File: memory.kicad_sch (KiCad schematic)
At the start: 18 parts, among them U2 MX25L4006EM2R-12G, U3 AT25SF128A-SHB-T

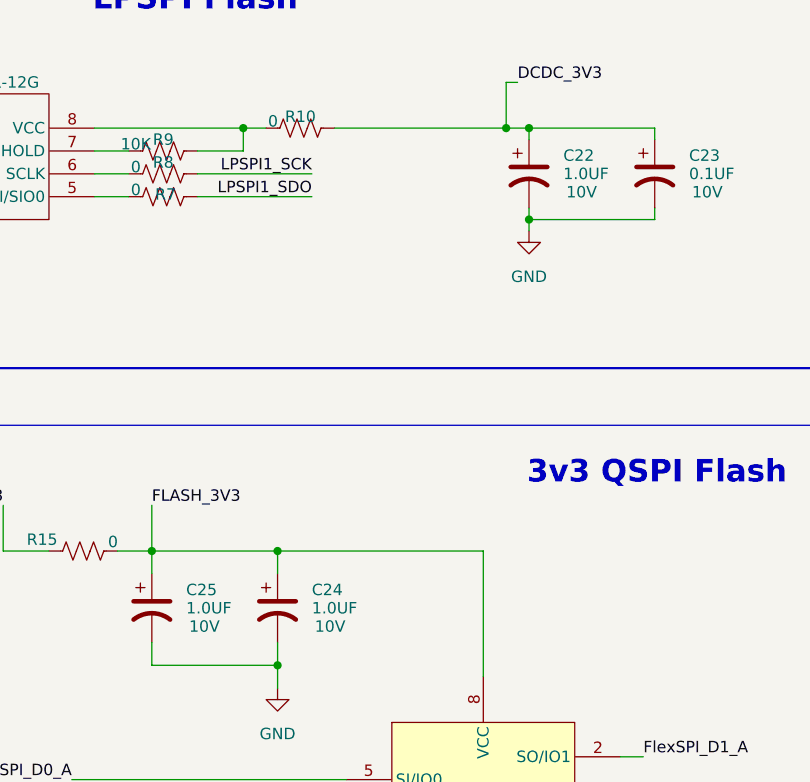
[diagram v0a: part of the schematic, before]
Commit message: menambah lebih dari setengah footprint
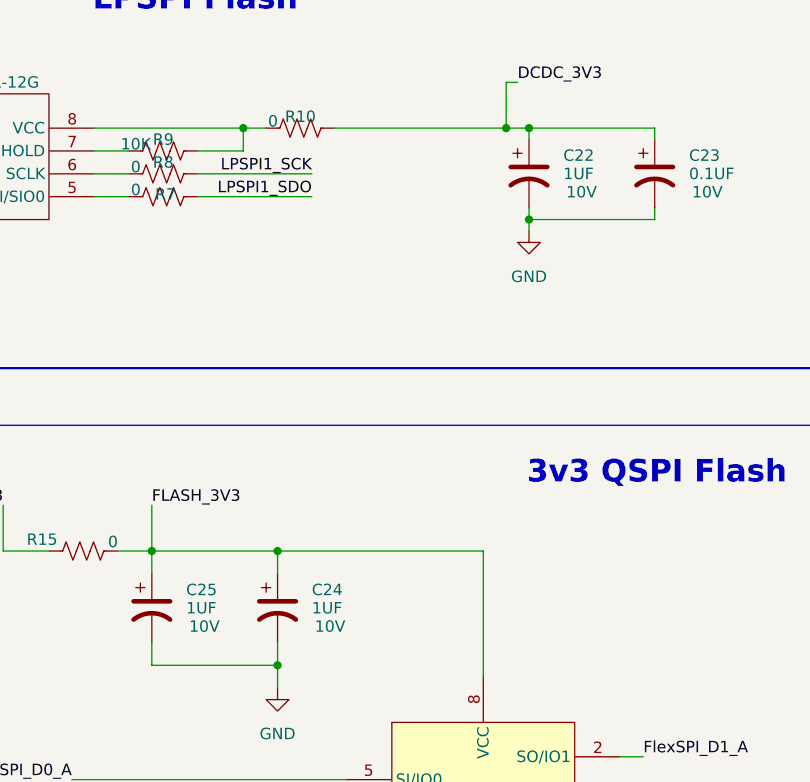
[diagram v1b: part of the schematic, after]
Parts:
- C22, C24, C25: value 1.0UF -> 1UF; footprint (none) -> Capacitor_SMD:C_0402_1005Metric
- C23: footprint (none) -> Capacitor_SMD:C_0402_1005Metric; MANUFACTURER (none) -> CC0402KRX5R6BB104
- R10, R11, R12, R13, R14, R15, R16, R17, R18, R7, R8, R9: footprint (none) -> Resistor_SMD:R_0402_1005Metric
- U2: footprint (none) -> Package_SON:WSON-8-1EP_6x5mm_P1.27mm_EP3.4x4.3mm; DigikeyPartNumber (none) -> MX25L4006EZNI-12G; MANUFACTURER (none) -> MX25L4006EZNI-12G
- U3: footprint (none) -> AT25SF128A_SHB_T:IC8_AT25SF128A-SHB-T_ADO; MANUFACTURER (none) -> AT25SF128A-SHB-T
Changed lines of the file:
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@@
 			)
 		)
-		(property "Footprint" ""
+		(property "Footprint" "AT25SF128A_SHB_T:IC8_AT25SF128A-SHB-T_ADO"
 			(at 229.87 129.54 0)
 			(effects
@@
 			)
 		)
+		(property "DigikeyPartNumber" ""
+			(at 229.87 129.54 0)
+			(effects
+				(font
+					(size 1.27 1.27)
+				)
+				(hide yes)
+			)
+		)
+		(property "MANUFACTURER" "AT25SF128A-SHB-T"
+			(at 229.87 129.54 0)
+			(effects
+				(font
+					(size 1.27 1.27)
+				)
+				(hide yes)
+			)
+		)
 		(pin "8"
 		)
@@
 			)
 		)
-		(property "Footprint" ""
+		(property "Footprint" "Resistor_SMD:R_0402_1005Metric"
 			(at 194.564 56.134 90)
 			(effects
@@
 			)
 		)
+		(property "DigikeyPartNumber" ""
+			(at 194.31 57.15 0)
+			(effects
+				(font
+					(size 1.27 1.27)
+				)
+				(hide yes)
+			)
+		)
 		(pin "1"
 		)
@@
 			)
 		)
-		(property "Footprint" ""
+		(property "Footprint" "Resistor_SMD:R_0402_1005Metric"
 			(at 143.764 48.514 90)
 			(effects
@@
 			)
 		)
+		(property "DigikeyPartNumber" ""
+			(at 143.51 49.53 0)
+			(effects
+				(font
+					(size 1.27 1.27)
+				)
+				(hide yes)
+			)
+		)
 		(pin "2"
 		)
@@
 			)
 		)
-		(property "Footprint" ""
+		(property "Footprint" "Resistor_SMD:R_0402_1005Metric"
 			(at 210.566 141.224 90)
 			(effects
@@
 					(size 1.27 1.27)
 				)
+			)
+		)
+		(property "DigikeyPartNumber" ""
+			(at 209.55 140.97 0)
+			(effects
+				(font
+					(size 1.27 1.27)
+				)
+				(hide yes)
 			)
 		)
@@
 			)
 		)
-		(property "Footprint" ""
+		(property "Footprint" "Capacitor_SMD:C_0402_1005Metric"
 			(at 248.92 54.61 0)
 			(effects
@@
 			)
 		)
+		(property "DigikeyPartNumber" ""
+			(at 248.92 54.61 0)
+			(effects
+				(font
+					(size 1.27 1.27)
+				)
+				(hide yes)
+			)
+		)
+		(property "MANUFACTURER" "CC0402KRX5R6BB104"
+			(at 248.92 54.61 0)
+			(effects
+				(font
+					(size 1.27 1.27)
+				)
+				(hide yes)
+			)
+		)
 		(pin "1"
 		)
@@
 			)
 		)
-		(property "Footprint" ""
+		(property "Footprint" "Resistor_SMD:R_0402_1005Metric"
 			(at 143.764 53.594 90)
 			(effects
@@
 		)
 		(property "Description" "Resistor, US symbol"
+			(at 143.51 54.61 0)
+			(effects
+				(font
+					(size 1.27 1.27)
+				)
+				(hide yes)
+			)
+		)
+		(property "DigikeyPartNumber" ""
 			(at 143.51 54.61 0)
 			(effects
@@
 			)
 		)
-		(property "Value" "1.0UF"
+		(property "Value" "1UF"
 			(at 238.76 54.61 0)
 			(effects
@@
 			)
 		)
-		(property "Footprint" ""
+		(property "Footprint" "Capacitor_SMD:C_0402_1005Metric"
 			(at 234.95 54.61 0)
 			(effects
@@
 					(size 1.27 1.27)
 				)
+			)
+		)
+		(property "DigikeyPartNumber" ""
+			(at 234.95 54.61 0)
+			(effects
+				(font
+					(size 1.27 1.27)
+				)
+				(hide yes)
 			)
 		)
@@
 			)
 		)
-		(property "Footprint" ""
+		(property "Footprint" "Resistor_SMD:R_0402_1005Metric"
 			(at 192.786 141.224 90)
 			(effects
@@
 			)
 		)
+		(property "DigikeyPartNumber" ""
+			(at 191.77 140.97 0)
+			(effects
+				(font
+					(size 1.27 1.27)
+				)
+				(hide yes)
+			)
+		)
 		(pin "1"
 		)
@@
 			)
 		)
-		(property "Footprint" ""
+		(property "Footprint" "Resistor_SMD:R_0402_1005Metric"
 			(at 194.564 53.594 90)
 			(effects
@@
 			)
 		)
+		(property "DigikeyPartNumber" ""
+			(at 194.31 54.61 0)
+			(effects
+				(font
+					(size 1.27 1.27)
+				)
+				(hide yes)
+			)
+		)
 		(pin "1"
 		)
@@
 			)
 		)
-		(property "Footprint" ""
+		(property "Footprint" "Resistor_SMD:R_0402_1005Metric"
 			(at 201.676 141.224 90)
 			(effects
@@
 			)
 		)
+		(property "DigikeyPartNumber" ""
+			(at 200.66 140.97 0)
+			(effects
+				(font
+					(size 1.27 1.27)
+				)
+				(hide yes)
+			)
+		)
 		(pin "1"
 		)
@@
 			)
 		)
-		(property "Footprint" ""
+		(property "Footprint" "Resistor_SMD:R_0402_1005Metric"
 			(at 143.764 45.974 90)
 			(effects
@@
 			)
 		)
+		(property "DigikeyPartNumber" ""
+			(at 143.51 46.99 0)
+			(effects
+				(font
+					(size 1.27 1.27)
+				)
+				(hide yes)
+			)
+		)
 		(pin "2"
 		)
@@
 			)
 		)
-		(property "Footprint" ""
+		(property "Footprint" "Resistor_SMD:R_0402_1005Metric"
 			(at 209.804 48.514 90)
 			(effects
@@
 			)
 		)
+		(property "DigikeyPartNumber" ""
+			(at 209.55 49.53 0)
+			(effects
+				(font
+					(size 1.27 1.27)
+				)
+				(hide yes)
+			)
+		)
 		(pin "1"
 		)
@@
 			)
 		)
-		(property "Value" "1.0UF"
+		(property "Value" "1UF"
 			(at 210.82 102.87 0)
 			(effects
@@
 			)
 		)
-		(property "Footprint" ""
+		(property "Footprint" "Capacitor_SMD:C_0402_1005Metric"
 			(at 207.01 102.87 0)
 			(effects
@@
 			)
 		)
+		(property "DigikeyPartNumber" ""
+			(at 207.01 102.87 0)
+			(effects
+				(font
+					(size 1.27 1.27)
+				)
+				(hide yes)
+			)
+		)
 		(pin "1"
 		)
@@
 			)
 		)
-		(property "Value" "1.0UF"
+		(property "Value" "1UF"
 			(at 196.85 102.87 0)
 			(effects
@@
 			)
 		)
-		(property "Footprint" ""
+		(property "Footprint" "Capacitor_SMD:C_0402_1005Metric"
 			(at 193.04 102.87 0)
 			(effects
@@
 			)
 		)
+		(property "DigikeyPartNumber" ""
+			(at 193.04 102.87 0)
+			(effects
+				(font
+					(size 1.27 1.27)
+				)
+				(hide yes)
+			)
+		)
 		(pin "1"
 		)
@@
 			)
 		)
-		(property "Footprint" ""
+		(property "Footprint" "Resistor_SMD:R_0402_1005Metric"
 			(at 185.674 95.504 90)
 			(effects
@@
 		)
 		(property "Description" "Resistor, US symbol"
+			(at 185.42 96.52 0)
+			(effects
+				(font
+					(size 1.27 1.27)
+				)
+				(hide yes)
+			)
+		)
+		(property "DigikeyPartNumber" ""
 			(at 185.42 96.52 0)
 			(effects
@@
 			)
 		)
-		(property "Footprint" ""
+		(property "Footprint" "Package_SON:WSON-8-1EP_6x5mm_P1.27mm_EP3.4x4.3mm"
 			(at 172.72 54.61 0)
 			(effects
@@
 			)
 		)
-		(property "Description" ""
+		(property "Description" "MX25L4006EZNI-12G"
 			(at 172.72 54.61 0)
+			(effects
+				(font
+					(size 1.27 1.27)
+				)
+				(hide yes)
+			)
+		)
+		(property "DigikeyPartNumber" "MX25L4006EZNI-12G"
+			(at 171.45 53.34 0)
+			(effects
+				(font
+					(size 1.27 1.27)
+				)
+				(hide yes)
+			)
+		)
+		(property "MANUFACTURER" "MX25L4006EZNI-12G"
+			(at 171.45 53.34 0)
 			(effects
 				(font
@@
 			)
 		)
-		(property "Footprint" ""
+		(property "Footprint" "Resistor_SMD:R_0402_1005Metric"
 			(at 194.564 51.054 90)
 			(effects
@@
 			)
 		)
+		(property "DigikeyPartNumber" ""
+			(at 194.31 52.07 0)
+			(effects
+				(font
+					(size 1.27 1.27)
+				)
+				(hide yes)
+			)
+		)
 		(pin "1"
 		)
@@
 			)
 		)
-		(property "Footprint" ""
+		(property "Footprint" "Resistor_SMD:R_0402_1005Metric"
 			(at 143.764 51.054 90)
 			(effects
@@
 			(at 143.51 52.07 0)
 			(effects
+				(font
+					(size 1.27 1.27)
+				)
+				(hide yes)
+			)
+		)
+		(property "DigikeyPartNumber" ""
+			(at 143.51 52.07 0)
+			(effects

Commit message: da
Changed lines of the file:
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@@
 		)
 	)
-	(label "DCDC_3V3"
+	(global_label "DCDC_3V3"
+		(shape input)
+		(at 125.73 43.18 180)
+		(fields_autoplaced yes)
+		(effects
+			(font
+				(size 1.27 1.27)
+			)
+			(justify right)
+		)
+		(property "Intersheetrefs" "${INTERSHEET_REFS}"
+			(at 113.1896 43.18 0)
+			(effects
+				(font
+					(size 1.27 1.27)
+				)
+				(justify right)
+				(hide yes)
+			)
+		)
+	)
+	(global_label "FLASH_3V3"
+		(shape input)
+		(at 193.04 91.44 0)
+		(fields_autoplaced yes)
+		(effects
+			(font
+				(size 1.27 1.27)
+			)
+			(justify left)
+		)
+		(property "Intersheetrefs" "${INTERSHEET_REFS}"
+			(at 206.2457 91.44 0)
+			(effects
+				(font
+					(size 1.27 1.27)
+				)
+				(justify left)
+				(hide yes)
+			)
+		)
+	)
+	(global_label "DCDC_3V3"
+		(shape input)
+		(at 233.68 44.45 0)
+		(fields_autoplaced yes)
+		(effects
+			(font
+				(size 1.27 1.27)
+			)
+			(justify left)
+		)
+		(property "Intersheetrefs" "${INTERSHEET_REFS}"
+			(at 246.2204 44.45 0)
+			(effects
+				(font
+					(size 1.27 1.27)
+				)
+				(justify left)
+				(hide yes)
+			)
+		)
+	)
+	(global_label "FlexSPI_CLK_A"
+		(shape input)
+		(at 184.15 124.46 180)
+		(fields_autoplaced yes)
+		(effects
+			(font
+				(size 1.27 1.27)
+			)
+			(justify right)
+		)
+		(property "Intersheetrefs" "${INTERSHEET_REFS}"
+			(at 167.6181 124.46 0)
+			(effects
+				(font
+					(size 1.27 1.27)
+				)
+				(justify right)
+				(hide yes)
+			)
+		)
+	)
+	(global_label "FlexSPI_D3_A"
+		(shape input)
+		(at 184.15 132.08 180)
+		(fields_autoplaced yes)
+		(effects
+			(font
+				(size 1.27 1.27)
+			)
+			(justify right)
+		)
+		(property "Intersheetrefs" "${INTERSHEET_REFS}"
+			(at 168.7067 132.08 0)
+			(effects
+				(font
+					(size 1.27 1.27)
+				)
+				(justify right)
+				(hide yes)
+			)
+		)
+	)
+	(global_label "DCDC_3V3"
+		(shape input)
 		(at 176.53 91.44 180)
 		(fields_autoplaced yes)
@@
 				(size 1.27 1.27)
 			)
-			(justify right bottom)
-		)
-	)
-	(label "FLASH_3V3"
-		(at 193.04 91.44 0)
-		(fields_autoplaced yes)
-		(effects
-			(font
-				(size 1.27 1.27)
-			)
-			(justify left bottom)
-		)
-	)
-	(label "FlexSPI_D3_A"
-		(at 184.15 132.08 180)
-		(fields_autoplaced yes)
-		(effects
-			(font
-				(size 1.27 1.27)
-			)
-			(justify right bottom)
-		)
-	)
-	(label "FlexSPI_SS0"
+			(justify right)
+		)
+		(property "Intersheetrefs" "${INTERSHEET_REFS}"
+			(at 163.9896 91.44 0)
+			(effects
+				(font
+					(size 1.27 1.27)
+				)
+				(justify right)
+				(hide yes)
+			)
+		)
+	)
+	(global_label "FlexSPI_D1_A"
+		(shape input)
+		(at 247.65 119.38 0)
+		(fields_autoplaced yes)
+		(effects
+			(font
+				(size 1.27 1.27)
+			)
+			(justify left)
+		)
+		(property "Intersheetrefs" "${INTERSHEET_REFS}"
+			(at 263.0933 119.38 0)
+			(effects
+				(font
+					(size 1.27 1.27)
+				)
+				(justify left)
+				(hide yes)
+			)
+		)
+	)
+	(global_label "LPSPI1_SCK"
+		(shape input)
+		(at 210.82 54.61 180)
+		(fields_autoplaced yes)
+		(effects
+			(font
+				(size 1.27 1.27)
+			)
+			(justify right)
+		)
+		(property "Intersheetrefs" "${INTERSHEET_REFS}"
+			(at 196.5258 54.61 0)
+			(effects
+				(font
+					(size 1.27 1.27)
+				)
+				(justify right)
+				(hide yes)
+			)
+		)
+	)
+	(global_label "FlexSPI_D2_A"
+		(shape input)
+		(at 184.15 129.54 180)
+		(fields_autoplaced yes)
+		(effects
+			(font
+				(size 1.27 1.27)
+			)
+			(justify right)
+		)
+		(property "Intersheetrefs" "${INTERSHEET_REFS}"
+			(at 168.7067 129.54 0)
+			(effects
+				(font
+					(size 1.27 1.27)
+				)
+				(justify right)
+				(hide yes)
+			)
+		)
+	)
+	(global_label "LPSPI1_SDI"
+		(shape input)
+		(at 120.65 52.07 0)
+		(fields_autoplaced yes)
+		(effects
+			(font
+				(size 1.27 1.27)
+			)
+			(justify left)
+		)
+		(property "Intersheetrefs" "${INTERSHEET_REFS}"
+			(at 134.279 52.07 0)
+			(effects
+				(font
+					(size 1.27 1.27)
+				)
+				(justify left)
+				(hide yes)
+			)
+		)
+	)
+	(global_label "LPSPI1_PCS0"
+		(shape input)
+		(at 120.65 49.53 0)
+		(fields_autoplaced yes)
+		(effects
+			(font
+				(size 1.27 1.27)
+			)
+			(justify left)
+		)
+		(property "Intersheetrefs" "${INTERSHEET_REFS}"
+			(at 136.1537 49.53 0)
+			(effects
+				(font
+					(size 1.27 1.27)
+				)
+				(justify left)
+				(hide yes)
+			)
+		)
+	)
+	(global_label "FlexSPI_SS0"
+		(shape input)
 		(at 184.15 127 180)
 		(fields_autoplaced yes)
@@
 				(size 1.27 1.27)
 			)
-			(justify right bottom)
-		)
-	)
-	(label "FlexSPI_D0_A"
+			(justify right)
+		)
+		(property "Intersheetrefs" "${INTERSHEET_REFS}"
+			(at 169.6139 127 0)
+			(effects
+				(font
+					(size 1.27 1.27)
+				)
+				(justify right)
+				(hide yes)
+			)
+		)
+	)
+	(global_label "LPSPI1_SDO"
+		(shape input)
+		(at 210.82 57.15 180)
+		(fields_autoplaced yes)
+		(effects
+			(font
+				(size 1.27 1.27)
+			)
+			(justify right)
+		)
+		(property "Intersheetrefs" "${INTERSHEET_REFS}"
+			(at 196.4653 57.15 0)
+			(effects
+				(font
+					(size 1.27 1.27)
+				)
+				(justify right)
+				(hide yes)
+			)
+		)
+	)
+	(global_label "FlexSPI_D0_A"
+		(shape input)
 		(at 184.15 121.92 180)
 		(fields_autoplaced yes)
@@
 				(size 1.27 1.27)
 			)
-			(justify right bottom)
-		)
-	)
-	(label "LPSPI1_SDI"
-		(at 120.65 52.07 0)
-		(fields_autoplaced yes)
-		(effects
-			(font
-				(size 1.27 1.27)
-			)
-			(justify left bottom)
-		)
-	)
-	(label "DCDC_3V3"
-		(at 125.73 43.18 180)
-		(fields_autoplaced yes)
-		(effects
-			(font
-				(size 1.27 1.27)
-			)
-			(justify right bottom)
-		)
-	)
-	(label "FlexSPI_CLK_A"
-		(at 184.15 124.46 180)
-		(fields_autoplaced yes)
-		(effects
-			(font
-				(size 1.27 1.27)
-			)
-			(justify right bottom)
-		)
-	)
-	(label "FLASH_3V3"
+			(justify right)
+		)
+		(property "Intersheetrefs" "${INTERSHEET_REFS}"
+			(at 168.7067 121.92 0)
+			(effects
+				(font
+					(size 1.27 1.27)
+				)
+				(justify right)
+				(hide yes)
+			)
+		)
+	)
+	(global_label "FLASH_3V3"
+		(shape input)
 		(at 190.5 149.86 180)
 		(fields_autoplaced yes)
@@
 				(size 1.27 1.27)
 			)
-			(justify right bottom)
-		)
-	)
-	(label "LPSPI1_SCK"
-		(at 210.82 54.61 180)
-		(fields_autoplaced yes)
-		(effects
-			(font
-				(size 1.27 1.27)
-			)
-			(justify right bottom)
-		)
-	)
-	(label "DCDC_3V3"
-		(at 233.68 44.45 0)
-		(fields_autoplaced yes)
-		(effects
-			(font
-				(size 1.27 1.27)
-			)
-			(justify left bottom)
-		)
-	)
-	(label "FlexSPI_D1_A"
-		(at 247.65 119.38 0)
-		(fields_autoplaced yes)
-		(effects
-			(font
-				(size 1.27 1.27)
-			)
-			(justify left bottom)
-		)
-	)
-	(label "LPSPI1_SDO"
-		(at 210.82 57.15 180)
-		(fields_autoplaced yes)
-		(effects
-			(font
-				(size 1.27 1.27)
-			)
-			(justify right bottom)
-		)
-	)
-	(label "LPSPI1_PCS0"
-		(at 120.65 49.53 0)
-		(fields_autoplaced yes)
-		(effects
-			(font
-				(size 1.27 1.27)
-			)
-			(justify left bottom)
-		)
-	)
-	(label "FlexSPI_D2_A"
-		(at 184.15 129.54 180)
-		(fields_autoplaced yes)
-		(effects
-			(font
-				(size 1.27 1.27)
-			)
-			(justify right bottom)
-		)
-	)
+			(justify right)
+		)
+		(property "Intersheetrefs" "${INTERSHEET_REFS}"
+			(at 177.2943 149.86 0)
+			(effects
+				(font
+					(size 1.27 1.27)
+				)
+				(justify right)
+				(hide yes)
+			)
+		)
+	)
